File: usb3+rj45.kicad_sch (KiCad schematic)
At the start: 0 parts

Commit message: [#56643] Create buses for interfaces, assign buses to blocks
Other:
- company: (none) -> Antmicro Ltd.
- title: (none) -> Com Express 7 baseboard
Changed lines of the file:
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@@
 (kicad_sch (version 20230121) (generator eeschema)
   (paper "A3")
+  (title_block
+    (title "Com Express 7 baseboard")
+    (date "2024-03-22")
+    (rev "1.0.0")
+    (company "Antmicro Ltd.")
+  )
   (hierarchical_label "USBSS_B{USBSS}" (shape input) (at 360.68 127 0) (fields_autoplaced)
     (effects (font (size 1.27 1.27)) (justify left))

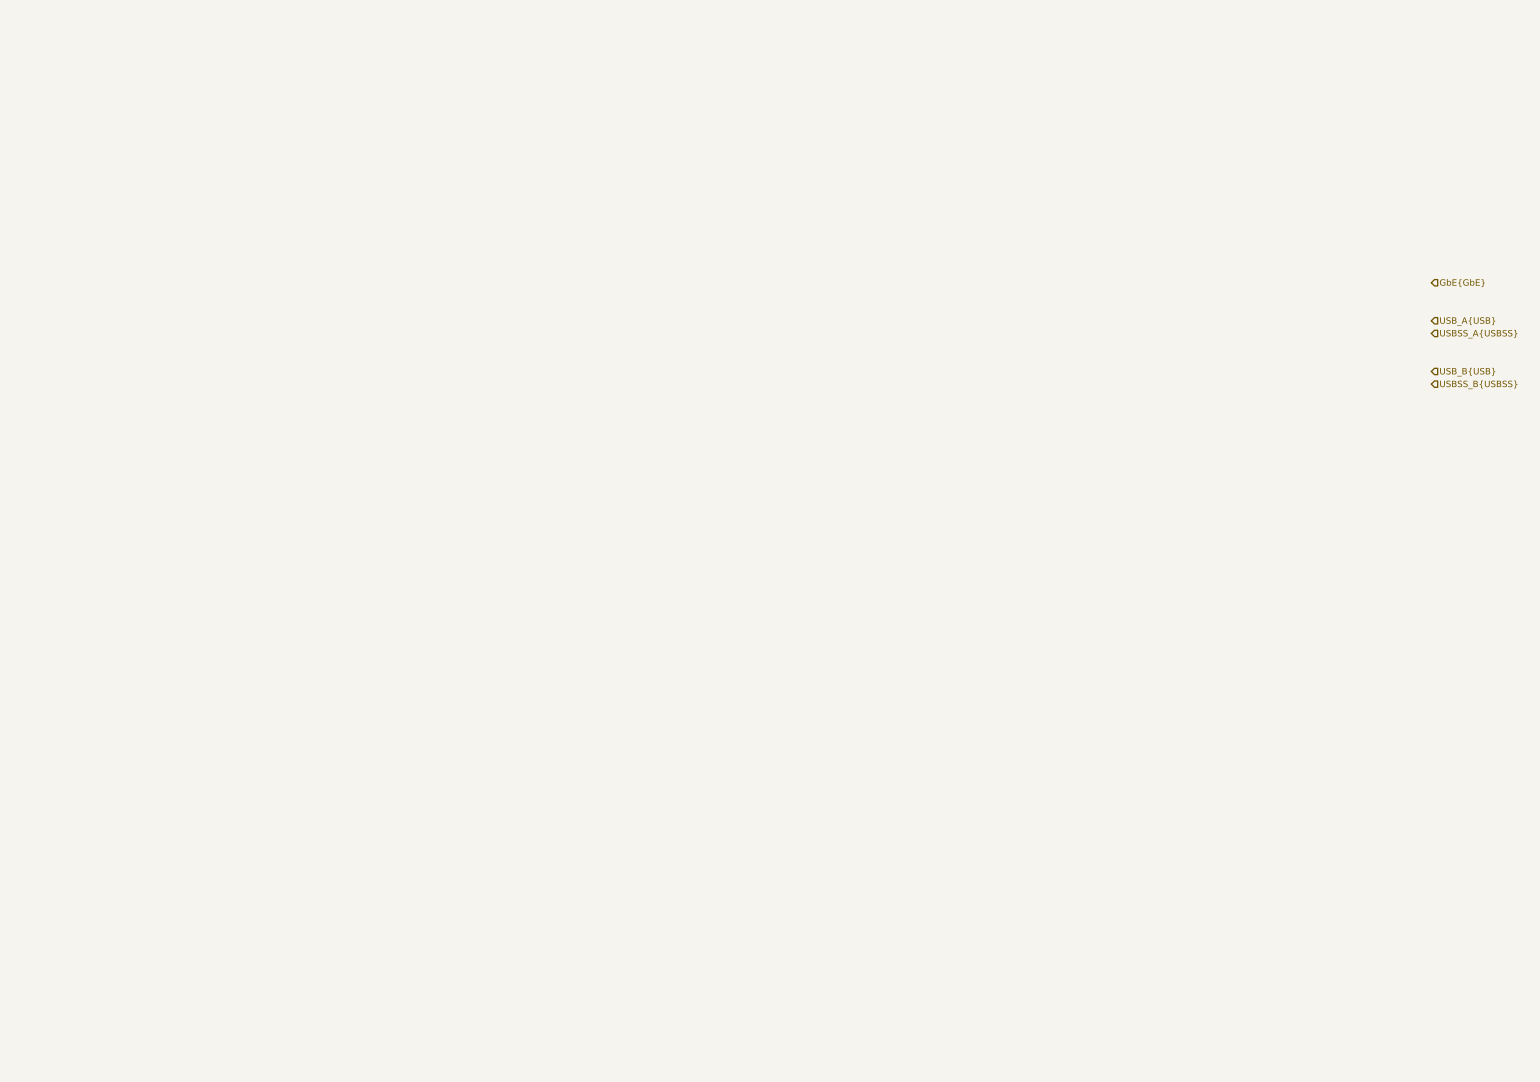
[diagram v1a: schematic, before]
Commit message: [#57056] Connect USB 3.0 connectors on combo connector
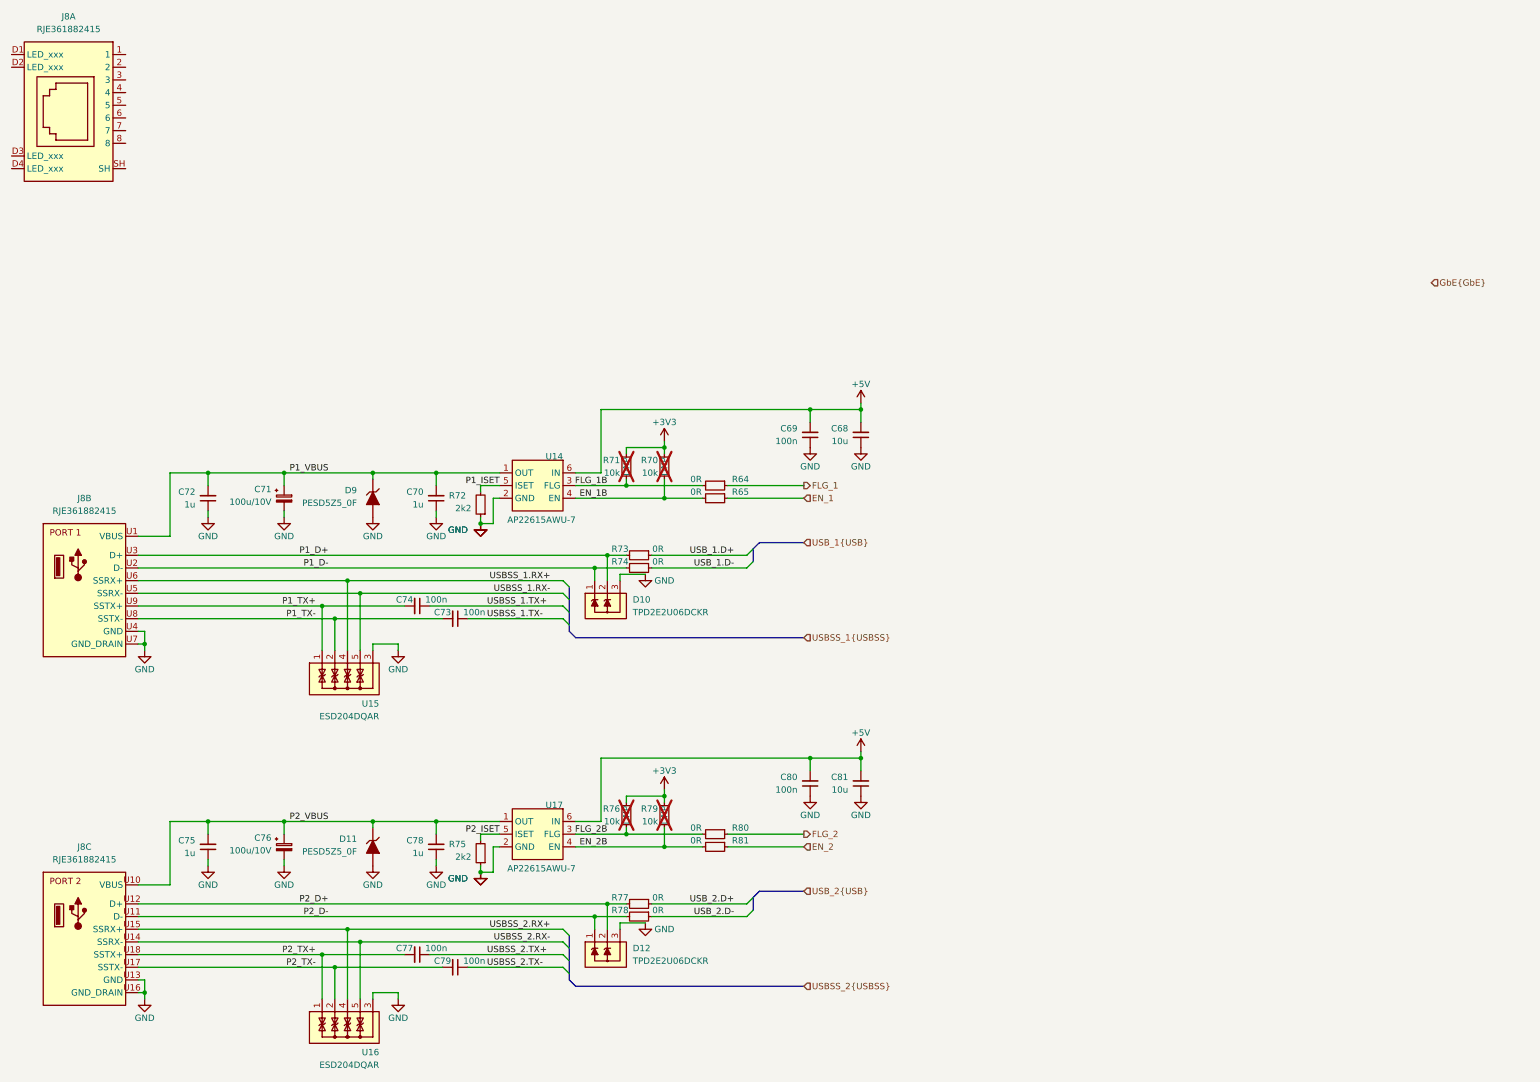
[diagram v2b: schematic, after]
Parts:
- added C68, C81: C_10u_0603, antmicro-footprints:C_0603_1608Metric, symbol antmicroCapacitors0603:C_10u_0603
- added C69, C73, C74, C77, C79, C80: C_100n_0402, antmicro-footprints:C_0402_1005Metric, symbol antmicroCapacitors0402:C_100n_0402
- added C70, C72, C75, C78: C_1u_0402, antmicro-footprints:C_0402_1005Metric, symbol antmicroCapacitors0402:C_1u_0402
- added C71, C76: C_Pol_100u_10V_KYOCERA-AVX-TLJ-A, antmicro-footprints:C_Pol_EIA-A, symbol antmicroCapacitorspol:C_Pol_100u_10V_KYOCERA-AVX-TLJ-A
- added D10, D12: TPD2E2U06DCKR, antmicro-footprints:SC70-3, symbol antmicroTVSDiodes:TPD2E2U06DCKR
- added D11, D9: PESD5Z5_0F, antmicro-footprints:SOD-523, symbol antmicroTVSDiodes:PESD5Z5_0F
- added J8: RJE361882415, symbol antmicroModularConnectorsJacks:Amphenol_RJE361882415
- added R64, R65, R73, R74, R77, R78, R80, R81: R_0R_0402, antmicro-footprints:R_0402_1005Metric, symbol antmicroResistors0402:R_0R_0402
- added R70, R71, R76, R79: R_10k_0402, antmicro-footprints:R_0402_1005Metric, symbol antmicroResistors0402:R_10k_0402
- added R72, R75: R_2k2_0402, antmicro-footprints:R_0402_1005Metric, symbol antmicroResistors0402:R_2k2_0402
- added U14, U17: AP22615A_TSOT26, antmicro-footprints:TSOT23-6, symbol antmicroPMICPowerDistributionSwitchesLoadDrivers:AP22615A_TSOT26
- added U15, U16: ESD204DQAR, antmicro-footprints:USON-10_2.5x1mm_P0.5mm, symbol antmicroTVSDiodes:ESD204DQAR
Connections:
- new net +3V3: R70.2, R71.2, R76.2, R79.2
- new net +5V: C68.2, C69.2, C80.2, C81.2, U14.6 (IN), U17.6 (IN)
- new net EN_1: R65.1
- new net EN_1B: R65.2, R70.1, U14.4 (EN)
- new net EN_2: R81.1
- new net EN_2B: R79.1, R81.2, U17.4 (EN)
- new net FLG_1: R64.1
- new net FLG_1B: R64.2, R71.1, U14.3 (FLG)
- new net FLG_2: R80.1
- new net FLG_2B: R76.1, R80.2, U17.3 (FLG)
- new net GND: C68.1, C69.1, C70.1, C71.2, C72.1, C75.1, C76.2, C78.1, C80.1, C81.1, D10.3, D11.2, D12.3, D9.2, J8.U13 (GND), J8.U16 (GND_DRAIN), J8.U4 (GND), J8.U7 (GND_DRAIN), R72.1, R75.1, U14.2 (GND), U15.3, U15.8, U16.3, U16.8, U17.2 (GND)
- new net P1_D+: D10.2, J8.U3 (D+), R73.2
- new net P1_D-: D10.1, J8.U2 (D-), R74.2
- new net P1_ISET: R72.2, U14.5 (ISET)
- new net P1_TX+: C74.2, J8.U9 (SSTX+), U15.1, U15.10
- new net P1_TX-: C73.2, J8.U8 (SSTX-), U15.2, U15.9
- new net P1_VBUS: C70.2, C71.1, C72.2, D9.1, J8.U1 (VBUS), U14.1 (OUT)
- new net P2_D+: D12.2, J8.U12 (D+), R77.2
- new net P2_D-: D12.1, J8.U11 (D-), R78.2
- new net P2_ISET: R75.2, U17.5 (ISET)
- new net P2_TX+: C77.2, J8.U18 (SSTX+), U16.1, U16.10
- new net P2_TX-: C79.2, J8.U17 (SSTX-), U16.2, U16.9
- new net P2_VBUS: C75.2, C76.1, C78.2, D11.1, J8.U10 (VBUS), U17.1 (OUT)
- new net USBSS_1.RX+: J8.U6 (SSRX+), U15.4, U15.7
- new net USBSS_1.RX-: J8.U5 (SSRX-), U15.5, U15.6
- new net USBSS_1.TX+: C74.1
- new net USBSS_1.TX-: C73.1
- new net USBSS_2.RX+: J8.U15 (SSRX+), U16.4, U16.7
- new net USBSS_2.RX-: J8.U14 (SSRX-), U16.5, U16.6
- new net USBSS_2.TX+: C77.1
- new net USBSS_2.TX-: C79.1
- new net USB_1.D+: R73.1
- new net USB_1.D-: R74.1
- new net USB_2.D+: R77.1
- new net USB_2.D-: R78.1

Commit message: [#57056] Connect GbE
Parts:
- added C82, C84, C85, C86, C87: C_100n_0402, antmicro-footprints:C_0402_1005Metric, symbol antmicroCapacitors0402:C_100n_0402
- added C83: C_1n_1210_2kV, antmicro-footprints:C_1210_3225Metric, symbol antmicroCapacitorsmisc:C_1n_1210_2kV
- added R82: R_330R_0402, antmicro-footprints:R_0402_1005Metric, symbol antmicroResistors0402:R_330R_0402
- added R83, R84, R85, R86: R_75R_0402, antmicro-footprints:R_0402_1005Metric, symbol antmicroResistors0402:R_75R_0402
- added R87, R90, R91, R92, R93, R94, R97: R_0R_0402, antmicro-footprints:R_0402_1005Metric, symbol antmicroResistors0402:R_0R_0402
- added R88, R89, R98, R99: R_470R_0402, antmicro-footprints:R_0402_1005Metric, symbol antmicroResistors0402:R_470R_0402
- added T1, T2, T3, T4: Trans_SM453229-381N7Y, antmicro-footprints:Trans_Eth_4.7x3.3mm, symbol antmicroInterfaceDriversReceiversTransceivers:Trans_SM453229-381N7Y
- added T5, T6, T7, T8: Choke_SRF2012A-801Y, symbol antmicroCommonModeChokes:Choke_SRF2012A-801Y
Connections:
- net +3V3: now also R88.2, R89.2, R98.2, R99.2
- net GND: now also C82.2, C83.1, C84.2, C85.2, C86.2, C87.2, R82.2
- net DA+: now reaches J8.1
- net DA+: now also T5.2
- net DA-: now reaches J8.2
- net DA-: now also T5.3
- net DB+: now reaches J8.3
- net DB+: now also T6.2
- net DC+: now reaches J8.4
- net DC+: now also T7.2
- net DC-: now reaches J8.5
- net DC-: now also T7.3
- net DB-: now reaches J8.6
- net DB-: now also T6.3
- net DD+: now reaches J8.7
- net DD+: now also T8.2
- net DD-: now reaches J8.8
- net DD-: now also T8.3
- net at J8.D1 (LED_xxx): now also R94.2, R98.1
- net at J8.D2 (LED_xxx): now also R97.2, R99.1
- net at J8.D3 (LED_xxx): now also R89.1, R90.2, R93.2
- net at J8.D4 (LED_xxx): now also R88.1, R91.2, R92.2
- net SH: now reaches J8.SH
- net SH: now also C82.1, R82.1
- new net: C84.1, C85.1, C86.1, C87.1, R87.1, T1.3, T2.3, T3.3, T4.3
- new net: T3.1, T7.1
- new net: T3.2, T7.4
- new net: T4.1, T8.1
- new net: T4.2, T8.4
- new net: R84.2, T3.5
- new net: T1.1, T5.1
- new net: T1.2, T5.4
- new net: R86.2, T1.5
- new net: C83.2, R83.1, R84.1, R85.1, R86.1
- new net: T2.1, T6.1
- new net: T2.2, T6.4
- new net: R83.2, T4.5
- new net: R85.2, T2.5
- new net GbE.CTREF: R87.2
- new net GbE.MDI0+: T1.6
- new net GbE.MDI0-: T1.7
- new net GbE.MDI1+: T2.6
- new net GbE.MDI1-: T2.7
- new net GbE.MDI2+: T3.6
- new net GbE.MDI2-: T3.7
- new net GbE.MDI3+: T4.6
- new net GbE.MDI3-: T4.7
- new net ~{GBE0_ACT}: R94.1, R97.1
- new net ~{GBE0_LINK_1000}: R90.1, R92.1
- new net ~{GBE0_LINK_100}: R91.1, R93.1
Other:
- note added: "GbE RJ45"
- note added: "LED polarity missing from datasheet so we're ready for both"
- note added: "USB 3.0"
- moved on the sheet: C68, C69, C70, C71, C72, C73, C74, C75, C76, C77, C78, C79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

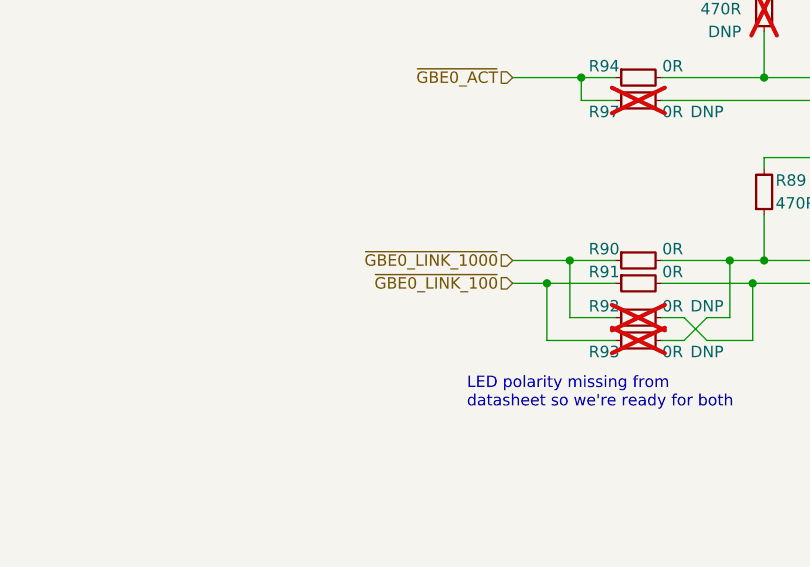
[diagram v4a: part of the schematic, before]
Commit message: [#57056] Update GPIO assignment
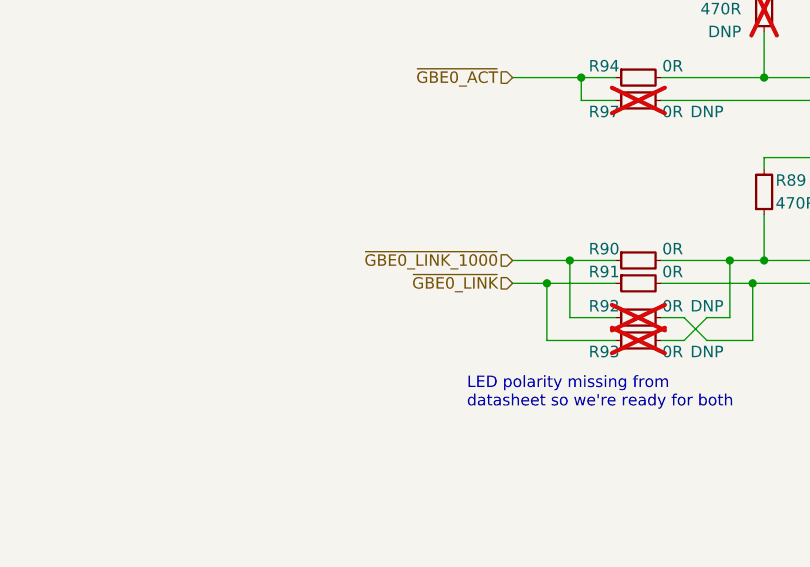
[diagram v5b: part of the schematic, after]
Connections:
- net ~{GBE0_LINK_100} renamed ~{GBE0_LINK}
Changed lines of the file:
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@@
     (effects (font (size 1.27 1.27)) (justify right))
   )
-  (hierarchical_label "~{GBE0_LINK_100}" (shape input) (at 100.33 86.36 180) (fields_autoplaced)
+  (hierarchical_label "~{GBE0_LINK}" (shape input) (at 100.33 86.36 180) (fields_autoplaced)
     (effects (font (size 1.27 1.27)) (justify right))
   )

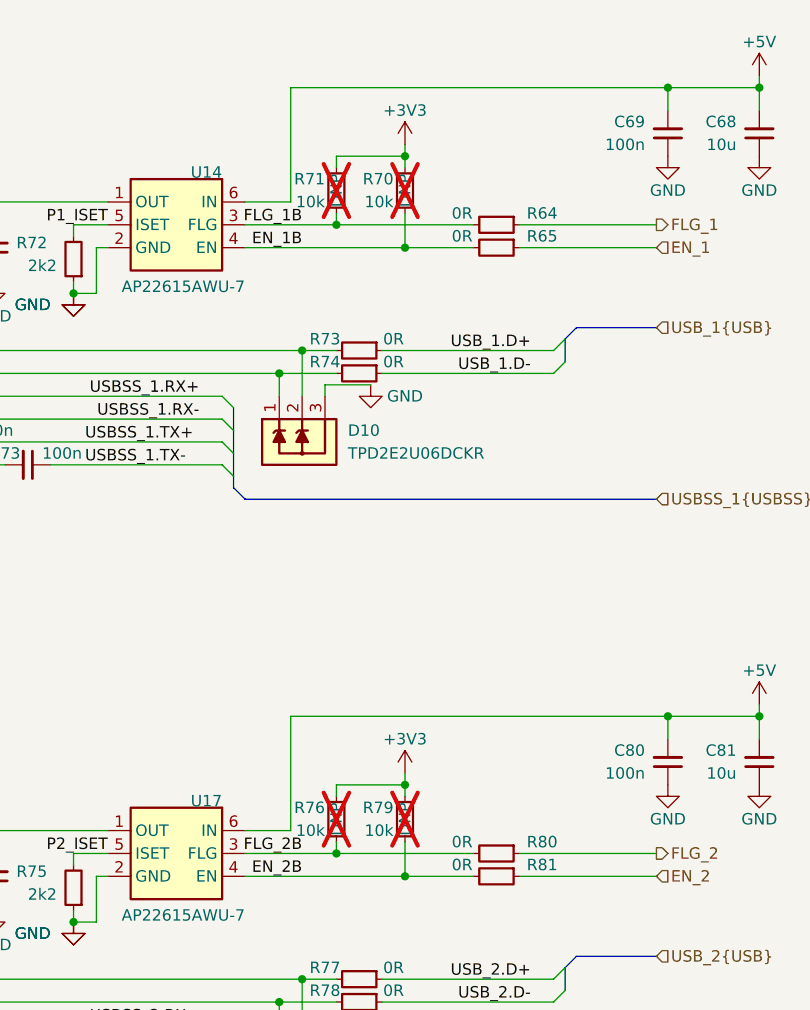
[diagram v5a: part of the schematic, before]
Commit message: [#57056] Add GPIO expander. Connect GPIOs and SMBus lines
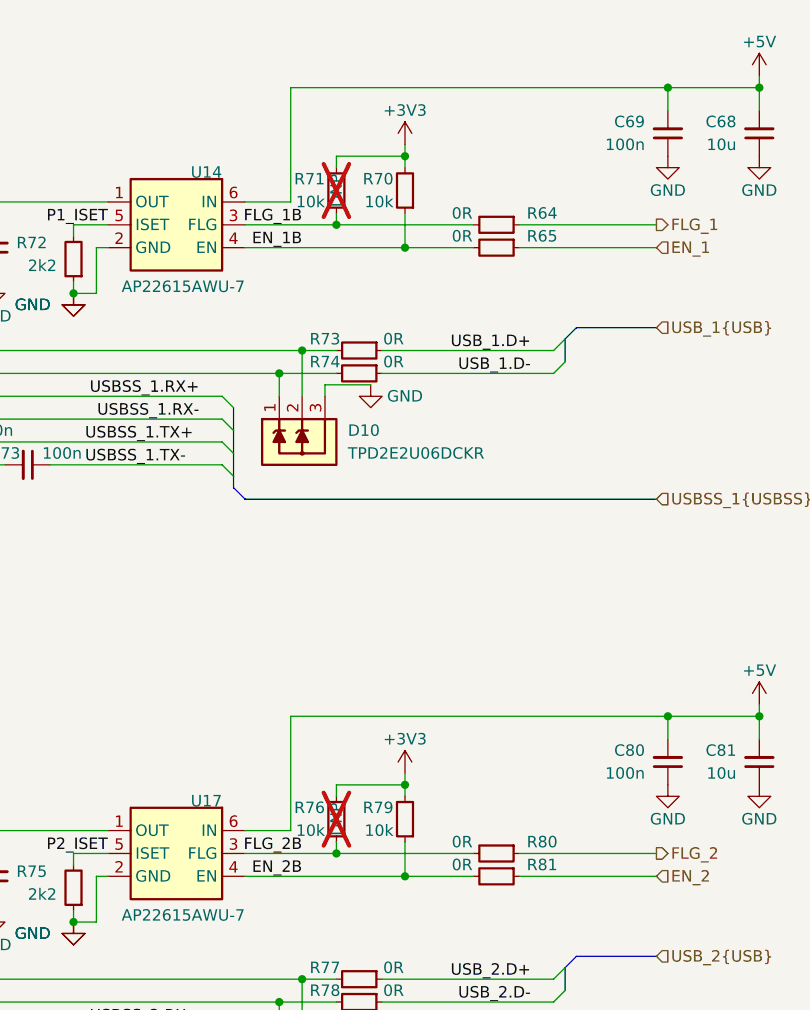
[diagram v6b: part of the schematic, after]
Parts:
- R70, R79: now fitted
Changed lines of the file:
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@@
   )
   (symbol (lib_id "antmicroResistors0402:R_10k_0402") (at 241.3 226.06 270) (mirror x) (unit 1)
-    (in_bom no) (on_board yes) (dnp yes)
+    (in_bom no) (on_board yes) (dnp no)
     (property "Reference" "R79" (at 240.03 222.25 90)
       (effects (font (size 1.27 1.27) (thickness 0.15)) (justify right))
@@
     )
     (property "DNP" "DNP" (at 241.3 223.52 0)
-      (effects (font (size 1.27 1.27)))
+      (effects (font (size 1.27 1.27)) hide)
     )
     (pin "1")
@@
   )
   (symbol (lib_id "antmicroResistors0402:R_10k_0402") (at 241.3 156.21 270) (mirror x) (unit 1)
-    (in_bom no) (on_board yes) (dnp yes)
+    (in_bom no) (on_board yes) (dnp no)
     (property "Reference" "R70" (at 240.03 152.4 90)
       (effects (font (size 1.27 1.27) (thickness 0.15)) (justify right))
@@
     )
     (property "DNP" "DNP" (at 241.3 153.67 0)
-      (effects (font (size 1.27 1.27)))
-    )
-    (pin "1")
+      (effects (font (size 1.27 1.27)) hide)
+    )
+    (pin "1")
